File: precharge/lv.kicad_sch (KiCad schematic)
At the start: 25 parts, among them K2 G5Q-1EU DC12, K3 G5Q-1EU DC12, Q4 BC846, Q5 BUK7M9R5-40H, Q6 XP262N7002TR-G, Q7 XP262N7002TR-G, U5 40106, U7 4013, U8 4071

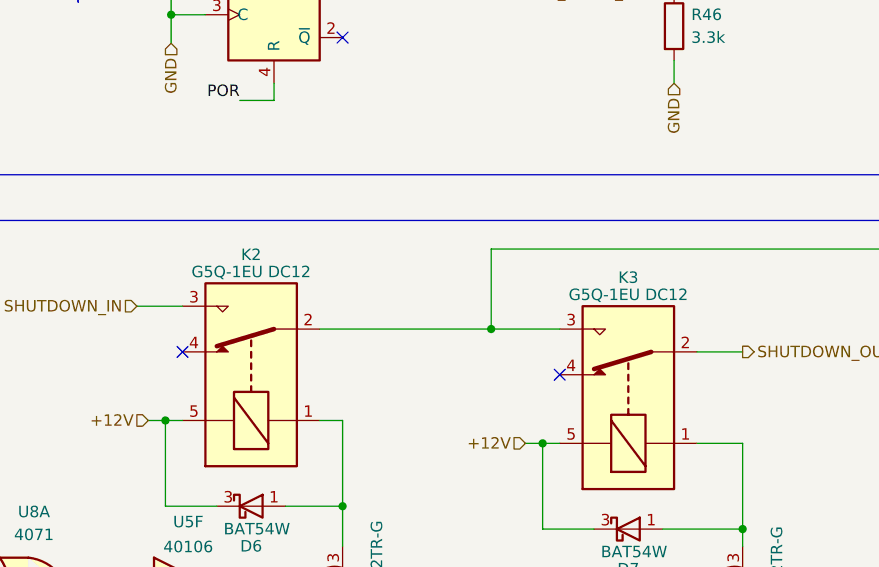
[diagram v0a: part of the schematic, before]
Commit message: chore(all) renamed BSPD files to remove version number from name, moved all symbols from individual symbol libraries into common/sufts-lib.kicad_sym, combined all project specific footprint folders into common/sufts-lib.pretty, moved all project specific step files into common/step, fixed all paths making them relative, fixed all broken cad models on pcbs. missing one cad model that is simply impossible to find online. imported discharge relay breakout pcb folder.
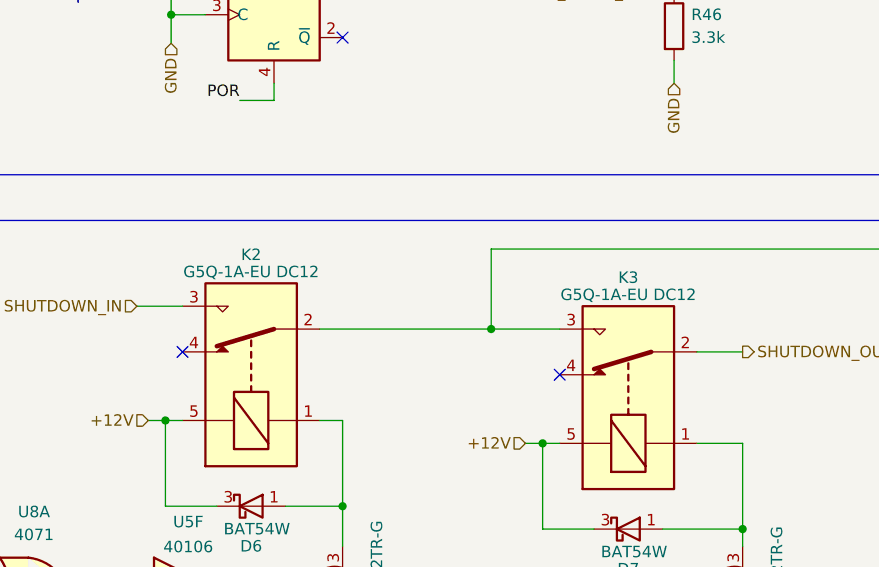
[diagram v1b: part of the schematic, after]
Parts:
- K2, K3: value G5Q-1EU DC12 -> G5Q-1A-EU DC12; footprint footprints:PCH-112L2MH -> SUFST:PCH-112L2MH
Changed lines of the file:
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@@
     (in_bom yes) (on_board yes)
     (property "Reference" "K2" (id 0) (at 65.405 97.155 90))
-    (property "Value" "G5Q-1EU DC12" (id 1) (at 65.405 99.06 90))
-    (property "Footprint" "footprints:PCH-112L2MH" (id 2) (at 66.675 99.06 0)
+    (property "Value" "G5Q-1A-EU DC12" (id 1) (at 65.405 99.06 90))
+    (property "Footprint" "SUFST:PCH-112L2MH" (id 2) (at 66.675 99.06 0)
       (effects (font (size 1.27 1.27)) (justify left) hide)
     )
@@
     (in_bom yes) (on_board yes)
     (property "Reference" "K3" (id 0) (at 107.315 99.695 90))
-    (property "Value" "G5Q-1EU DC12" (id 1) (at 107.315 101.6 90))
-    (property "Footprint" "footprints:PCH-112L2MH" (id 2) (at 108.585 101.6 0)
+    (property "Value" "G5Q-1A-EU DC12" (id 1) (at 107.315 101.6 90))
+    (property "Footprint" "SUFST:PCH-112L2MH" (id 2) (at 108.585 101.6 0)
       (effects (font (size 1.27 1.27)) (justify left) hide)
     )
